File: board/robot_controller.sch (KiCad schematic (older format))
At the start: 37 parts, among them U2 STM32F405-144

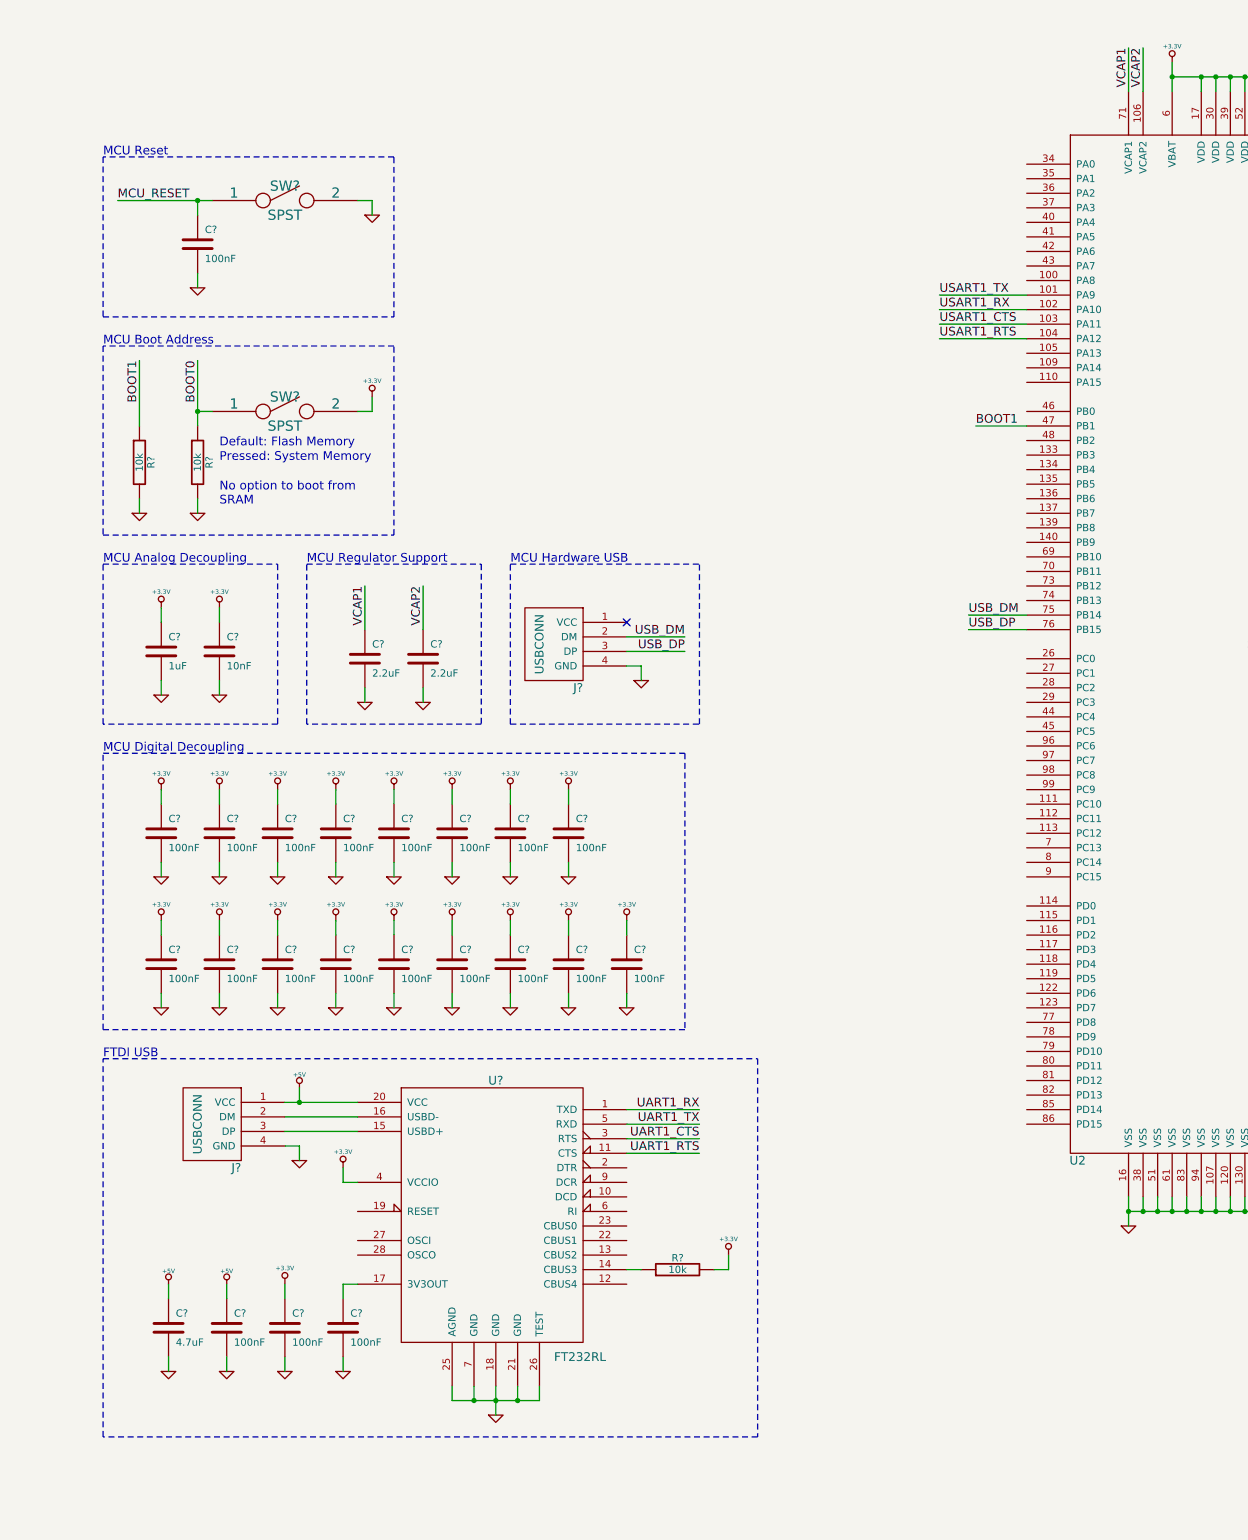
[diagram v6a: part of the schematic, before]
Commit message: FTDI Tx and Rx LEDs
I forgot to add the Tx and Rx LEDs for the FTDI chip.
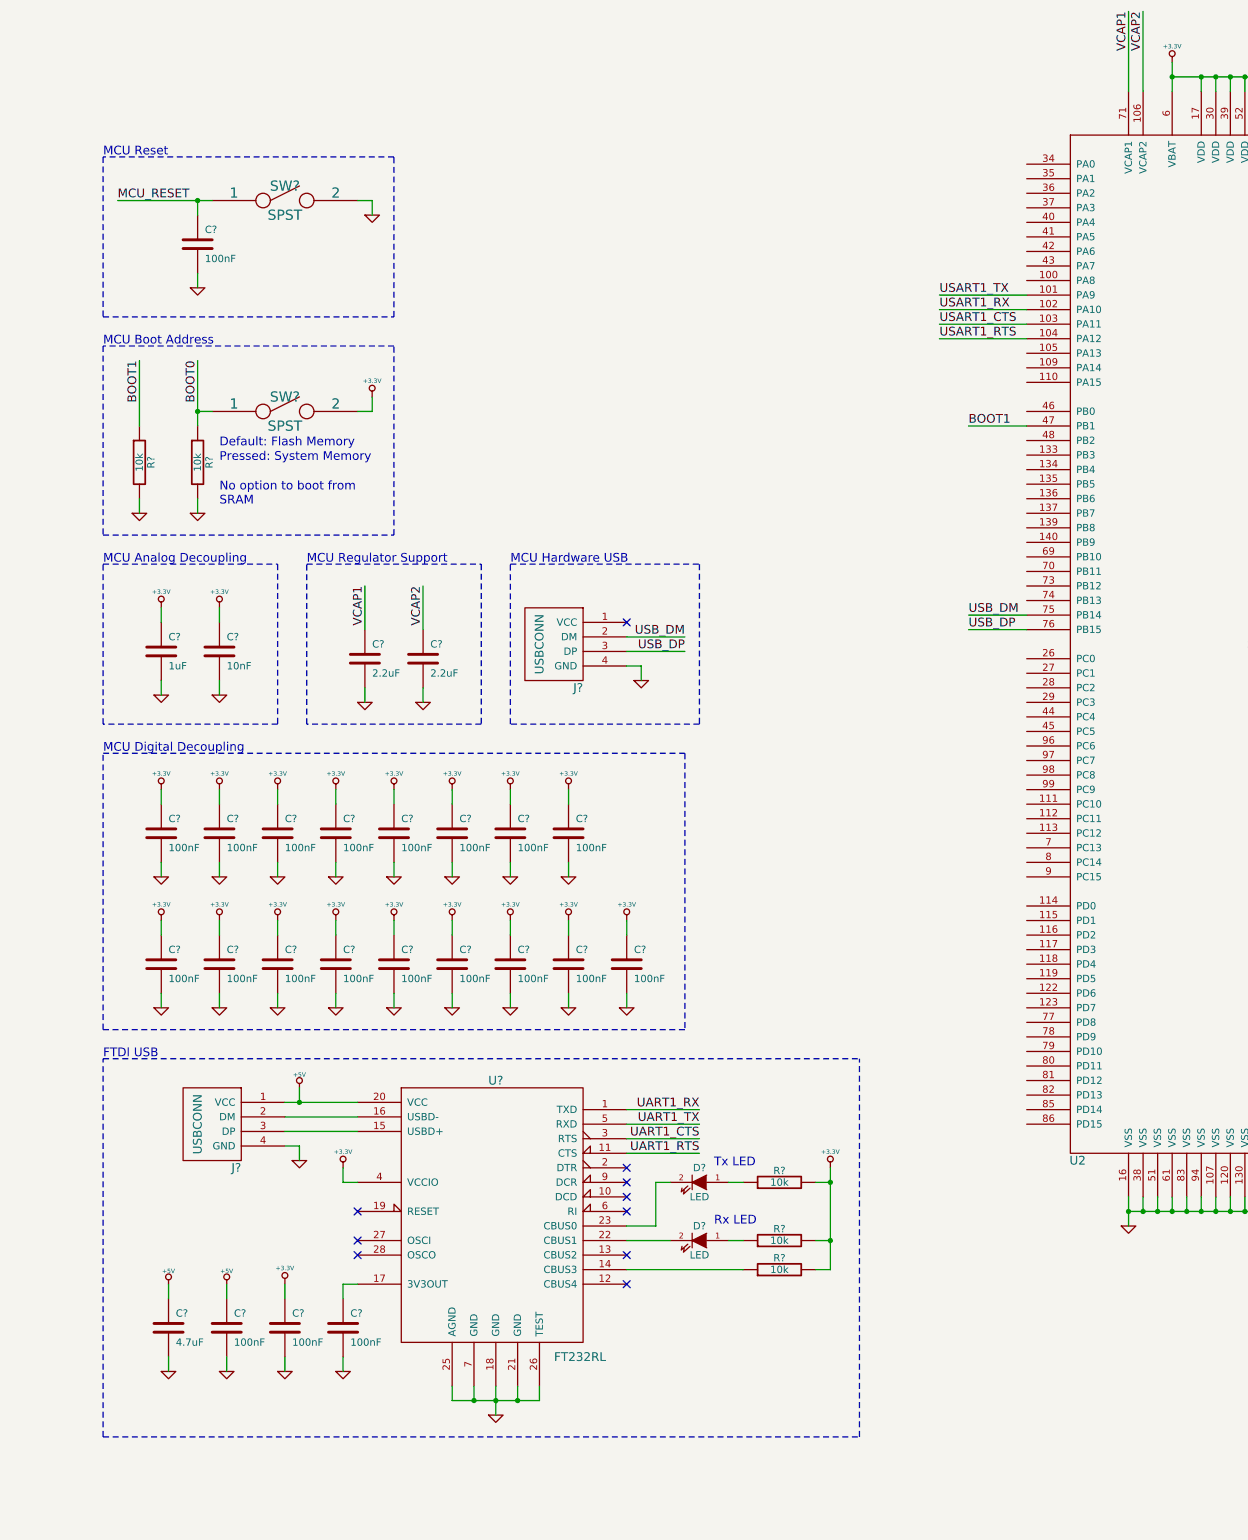
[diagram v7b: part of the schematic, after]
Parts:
- added D? (x2): LED, symbol LED
- added R? (x2): 10k, symbol R
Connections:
- net +3.3V: now also R?.2, R?.2
- net at U?.22 (CBUS1): now also D?.2 (K)
- net at U?.23 (CBUS0): now also D?.2 (K)
- new net: D?.1 (A), R?.1 (x2)
- no-connect marks 1 -> 10
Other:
- note added: "Rx LED"
- note added: "Tx LED"
- moved on the sheet: R?
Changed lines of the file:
@@
 Text Label 31850 16750 3    60   ~ 0
 VCAP2
-Text Label 36700 13050 3    60   ~ 0
+Text Label 36700 12800 3    60   ~ 0
 VCAP1
-Text Label 36800 13050 3    60   ~ 0
+Text Label 36800 12800 3    60   ~ 0
 VCAP2
 Text Notes 29650 13800 0    60   ~ 0
@@
 	1    0    0    -1
 $EndComp
-Text Label 35650 15650 0    60   ~ 0
+Text Label 35600 15650 0    60   ~ 0
 BOOT1
 Text Label 38900 12800 3    60   ~ 0
@@
 	31050 17700 31050 16600
 Wire Wire Line
-	36700 13050 36700 13350
-Wire Wire Line
-	36800 13050 36800 13350
+	36700 12800 36700 13350
+Wire Wire Line
+	36800 12800 36800 13350
 Wire Notes Line
 	29650 13800 29650 14900
@@
 	31650 13800 29650 13800
 Wire Wire Line
-	36000 15650 35650 15650
+	36000 15650 35600 15650
 Wire Wire Line
 	38900 12800 38900 13350
@@
 L +3.3V #PWR?
 U 1 1 52EDB4D7
-P 33950 21350
-F 0 "#PWR?" H 33950 21310 30  0001 C CNN
-F 1 "+3.3V" H 33950 21460 30  0000 C CNN
-F 2 "" H 33950 21350 60  0000 C CNN
-F 3 "" H 33950 21350 60  0000 C CNN
-	1    33950 21350
-	1    0    0    -1
-$EndComp
-Wire Wire Line
-	33950 21450 33950 21350
+P 34650 20750
+F 0 "#PWR?" H 34650 20710 30  0001 C CNN
+F 1 "+3.3V" H 34650 20860 30  0000 C CNN
+F 2 "" H 34650 20750 60  0000 C CNN
+F 3 "" H 34650 20750 60  0000 C CNN
+	1    34650 20750
+	1    0    0    -1
+$EndComp
+Wire Wire Line
+	34650 20750 34650 21450
 $Comp
 L R R?
 U 1 1 52EDB588
-P 33600 21450
-F 0 "R?" V 33680 21450 50  0000 C CNN
-F 1 "10k" V 33600 21450 50  0000 C CNN
-F 2 "" H 33600 21450 60  0000 C CNN
-F 3 "" H 33600 21450 60  0000 C CNN
-	1    33600 21450
+P 34300 21450
+F 0 "R?" V 34380 21450 50  0000 C CNN
+F 1 "10k" V 34300 21450 50  0000 C CNN
+F 2 "" H 34300 21450 60  0000 C CNN
+F 3 "" H 34300 21450 60  0000 C CNN
+	1    34300 21450
 	0    -1   -1   0
 $EndComp
@@
 	30900 21550 30900 21650
 Wire Wire Line
-	33250 21450 33350 21450
-Wire Wire Line
-	33850 21450 33950 21450
+	34650 21450 34550 21450
 Wire Wire Line
 	31300 20850 31400 20850
@@
 	30900 20500 31400 20500
 Wire Notes Line
-	29650 20000 34150 20000
-Wire Notes Line
-	34150 20000 34150 22600
-Wire Notes Line
-	34150 22600 29650 22600
+	29650 20000 34850 20000
+Wire Notes Line
+	34850 22600 34850 20000
+Wire Notes Line
+	29650 22600 34850 22600
 Wire Notes Line
 	29650 22600 29650 20000
@@
 	32450 16600 33750 16600
 Wire Notes Line
-	33750 17700 33750 16600
-Wire Notes Line
-	32450 17700 33750 17700
+	33750 16600 33750 17700
+Wire Notes Line
+	33750 17700 32450 17700
 Wire Notes Line
 	32450 17700 32450 16600
@@
 Text Label 33650 17200 2    60   ~ 0
 USB_DP
+NoConn ~ 31400 21050
+NoConn ~ 31400 21250
+NoConn ~ 31400 21350
+NoConn ~ 33250 20750
+NoConn ~ 33250 20850
+NoConn ~ 33250 20950
+NoConn ~ 33250 21050
+NoConn ~ 33250 21550
+NoConn ~ 33250 21350
+$Comp
+L LED D?
+U 1 1 52EF8A52
+P 33750 21250
+F 0 "D?" H 33750 21350 50  0000 C CNN
+F 1 "LED" H 33750 21150 50  0000 C CNN
+F 2 "" H 33750 21250 60  0000 C CNN
+F 3 "" H 33750 21250 60  0000 C CNN
+	1    33750 21250
+	-1   0    0    -1
+$EndComp
+$Comp
+L LED D?
+U 1 1 52EF9C76
+P 33750 20850
+F 0 "D?" H 33750 20950 50  0000 C CNN
+F 1 "LED" H 33750 20750 50  0000 C CNN
+F 2 "" H 33750 20850 60  0000 C CNN
+F 3 "" H 33750 20850 60  0000 C CNN
+	1    33750 20850
+	-1   0    0    -1
+$EndComp
+Wire Wire Line
+	33450 21150 33250 21150
+Wire Wire Line
+	33450 20850 33450 21150
+$Comp
+L R R?
+U 1 1 52EFAD14
+P 34300 20850
+F 0 "R?" V 34380 20850 50  0000 C CNN
+F 1 "10k" V 34300 20850 50  0000 C CNN
+F 2 "" H 34300 20850 60  0000 C CNN
+F 3 "" H 34300 20850 60  0000 C CNN
+	1    34300 20850
+	0    -1   -1   0
+$EndComp
+$Comp
+L R R?
+U 1 1 52EFAD1F
+P 34300 21250
+F 0 "R?" V 34380 21250 50  0000 C CNN
+F 1 "10k" V 34300 21250 50  0000 C CNN
+F 2 "" H 34300 21250 60  0000 C CNN
+F 3 "" H 34300 21250 60  0000 C CNN
+	1    34300 21250
+	0    -1   -1   0
+$EndComp
+Wire Wire Line
+	33950 20850 34050 20850
+Wire Wire Line
+	33950 21250 34050 21250
+Wire Wire Line
+	34550 21250 34650 21250
+Wire Wire Line
+	33550 21250 33250 21250
+Wire Wire Line
+	34050 21450 33250 21450
+Wire Wire Line
+	33550 20850 33450 20850
+Wire Wire Line
+	34650 20850 34550 20850
+Connection ~ 34650 21250
+Connection ~ 34650 20850
+Text Notes 33850 20750 0    60   ~ 0
+Tx LED
+Text Notes 33850 21150 0    60   ~ 0
+Rx LED
 $EndSCHEMATC

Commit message: SPI for Steppers and Temperature
I cleaned up the stepper driver section of the main schematic and
routed the high speed SPI interface over to it. I also got the second
SPI module connected to the temperature sensors.
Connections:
- net SPI2_MISO: now reaches U2.28 (PC2)
- net SPI2_MOSI: now reaches U2.29 (PC3)
- net SPI1_SCK: now reaches U2.41 (PA5)
- net SPI1_MISO: now reaches U2.42 (PA6)
- net SPI1_MOSI: now reaches U2.43 (PA7)
- net SPI2_SCK: now reaches U2.74 (PB13)
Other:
- note added: "Stepper Motor Driver Sense"
- note added: "Stepper Motor Drivers"
- note added: "Temperature Sensors"
- moved on the sheet: R?
